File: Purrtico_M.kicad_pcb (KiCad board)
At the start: 2 copper layers, 100 x 60 mm, 120 parts, among them J1 Conn_02x05_Odd_Even, J2 Conn_01x02, J4 Conn_01x02, U1 OPA1679, U2 OPA1679, U3 OPA1679

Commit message: update high shelf
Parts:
- C20: value 470p -> 220p
- C31: value 4n7 -> 2n2
- C34: value 68n -> 22n

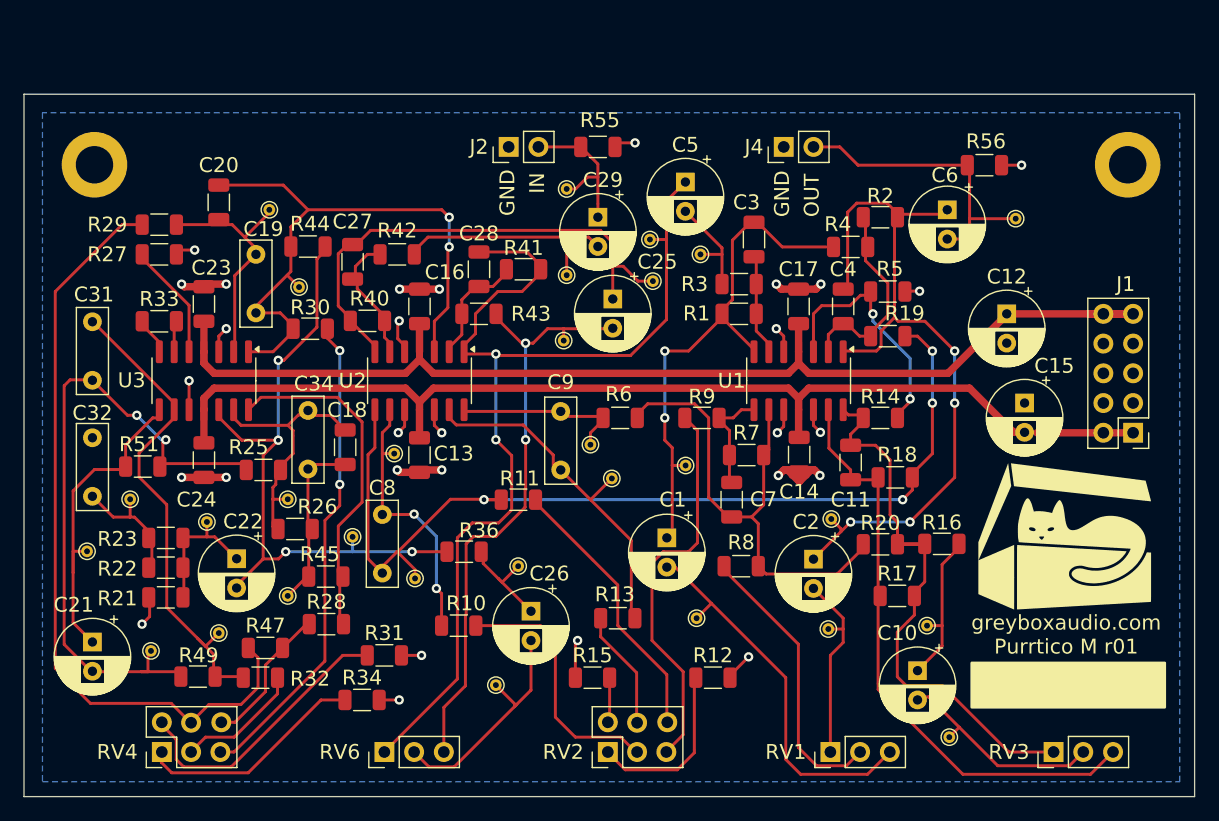
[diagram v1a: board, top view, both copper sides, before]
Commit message: added input gain control
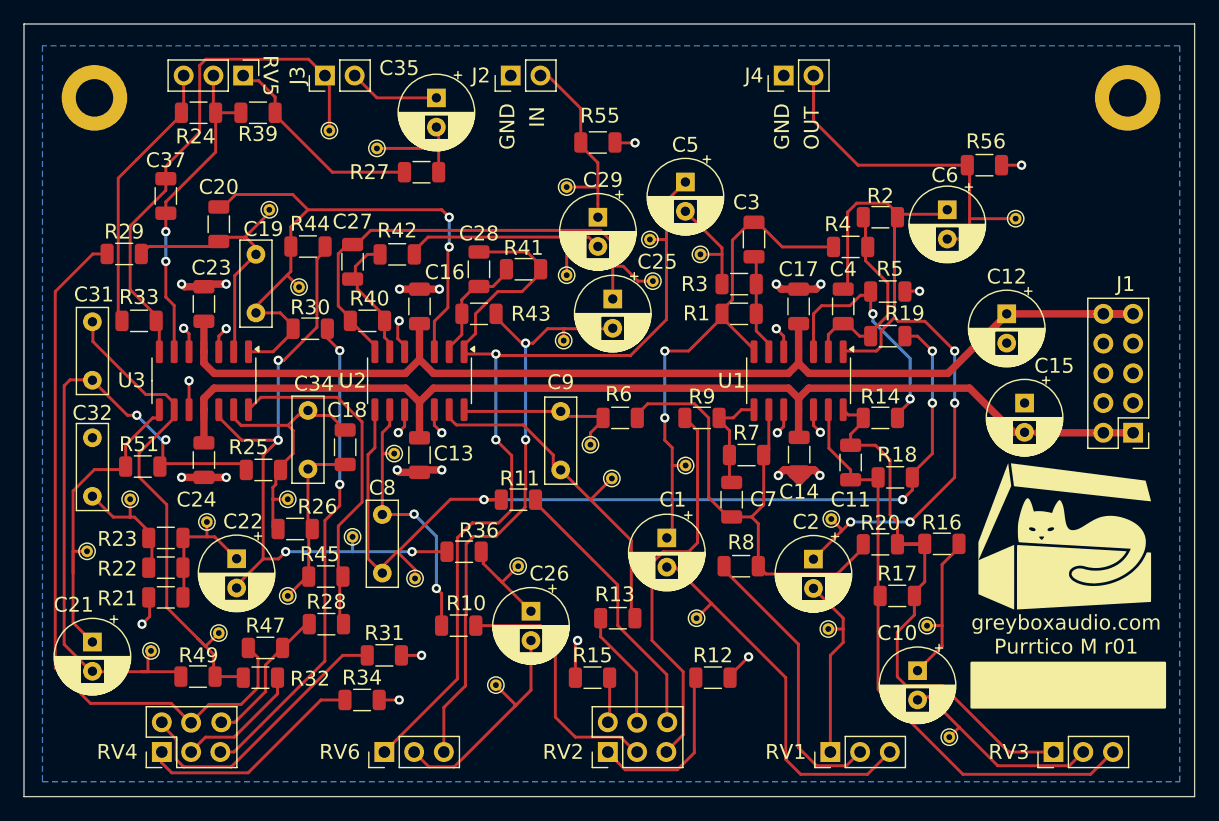
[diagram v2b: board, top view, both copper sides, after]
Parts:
- added C35: 100u, Capacitor_THT:CP_Radial_D6.3mm_P2.50mm, F.Cu at (113.0, 29.2)
- added C37: 22p, Capacitor_SMD:C_1206_3216Metric, F.Cu at (89.9, 37.6)
- added J3: Conn_01x02, Connector_PinHeader_2.54mm:PinHeader_1x02_P2.54mm_Vertical, F.Cu at (103.5, 27.3)
- added R24: 0R, Resistor_SMD:R_1206_3216Metric, F.Cu at (92.7, 30.5)
- added R39: 0R, Resistor_SMD:R_1206_3216Metric, F.Cu at (97.8, 30.5)
- added RV5: 5k log, Connector_PinHeader_2.54mm:PinHeader_1x03_P2.54mm_Vertical, F.Cu at (96.5, 27.3)
- added TP30: TestPoint, TestPoint:TestPoint_THTPad_D1.0mm_Drill0.5mm, F.Cu at (108.0, 33.5)
- added TP31: TestPoint, TestPoint:TestPoint_THTPad_D1.0mm_Drill0.5mm, F.Cu at (103.9, 32.0)
- R27, R33: value 0R -> 2k
- moved R27 23.5 mm to (111.8, 35.6)
- moved J2 6.10 mm to (119.4, 27.3)
- moved J4 6.09 mm to (142.7, 27.3)
- moved H1 5.71 mm to (83.8, 29.2)
- moved H2 5.71 mm to (172.1, 29.2)
- moved R29 3.91 mm to (86.4, 42.5)
- moved C20 1.87 mm to (94.4, 40.0)
- moved R33 1.73 mm to (87.6, 48.3), turned to 0 degrees
- moved R55 0.38 mm to (126.8, 33.0)
- moved TP1 0.16 mm to (124.2, 36.8)
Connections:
- R27 pad 1: GND -> Net-(C35-Pad2)
- R27 pad 2: Net-(U3B-+) -> Net-(R27-Pad2)
- R33 pad 1: Net-(U3B--) -> Net-(R24-Pad2)
- U3 pad 5: Net-(U3B-+) -> GND
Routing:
- net Net-(J3-Pin_1): track 2.07 -> 42.9 mm
- net Net-(U3B--): track 2.41 -> 27.6 mm, vias 0 -> 2
- net Net-(R24-Pad2): track 0.00 -> 22.5 mm
- net Net-(R27-Pad2): track 0.00 -> 17.7 mm
- net Net-(U3B-+): track 9.63 -> 0.00 mm
- net Net-(C35-Pad2): track 0.00 -> 8.93 mm
- net Net-(J3-Pin_2): track 0.00 -> 7.77 mm
- net Net-(J4-Pin_2): track 25.8 -> 30.6 mm
- net Net-(R29-Pad1): track 66.2 -> 62.2 mm
- net Net-(J2-Pin_2): track 13.3 -> 16.3 mm
- net Net-(U3A--): track 19.6 -> 21.6 mm
- net Net-(U3C--): track 40.4 -> 41.4 mm
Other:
- board size 100 x 60 mm -> 100 x 66 mm

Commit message: added 0R for mounting holes
as well as some small layout refinements
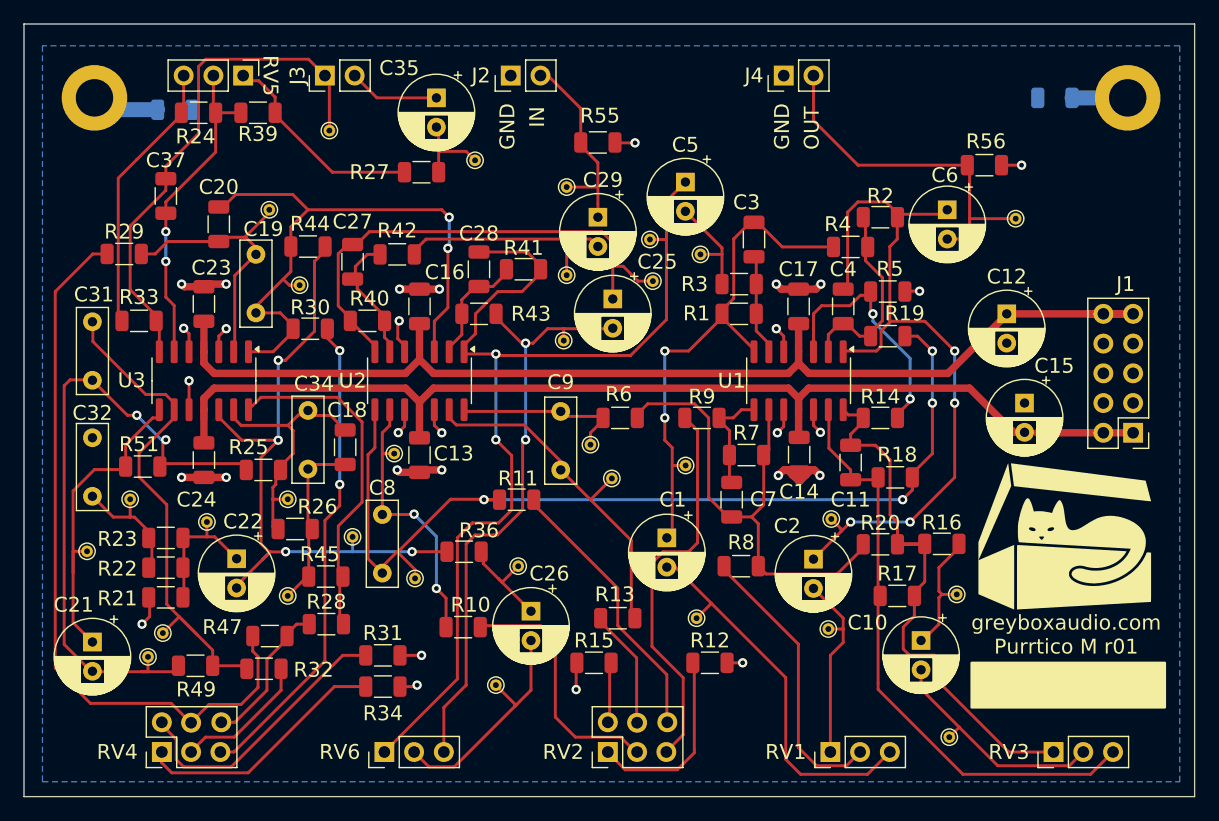
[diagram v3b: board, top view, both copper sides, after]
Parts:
- added R35: 0R, Resistor_SMD:R_1206_3216Metric, B.Cu at (90.7, 30.2)
- added R37: 0R, Resistor_SMD:R_1206_3216Metric, B.Cu at (165.9, 29.2)
- moved TP30 8.44 mm to (116.3, 34.5)
- moved TP20 4.78 mm to (89.7, 74.9)
- moved TP19 3.68 mm to (157.5, 71.6)
- moved C10 2.59 mm to (154.4, 75.6)
- moved R34 2.11 mm to (108.5, 79.5)
- moved R12 1.30 mm to (136.4, 77.5)
- moved R15 1.28 mm to (126.5, 77.5)
- moved R47 1.09 mm to (98.8, 75.2)
- moved R49 0.95 mm to (92.5, 77.7)
- moved R32 0.82 mm to (98.3, 78.0)
- moved TP17 0.57 mm to (88.4, 77.0)
- moved R10 0.40 mm to (115.3, 74.4)
- moved TP22 0.17 mm to (101.3, 45.2)
- moved R11 0.14 mm to (119.9, 63.5)
- moved R31 0.13 mm to (108.5, 76.8)
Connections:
- H1 pad 1: GND -> Net-(H1-Pad1)
- H2 pad 1: GND -> Net-(H2-Pad1)
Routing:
- net Net-(H2-Pad1): track 0.00 -> 4.76 mm
- net Net-(H1-Pad1): track 0.00 -> 4.38 mm
- net Net-(C10-Pad1): track 13.3 -> 10.9 mm
- net Net-(R34-Pad2): track 19.5 -> 21.8 mm
- net GND: track 61.3 -> 59.3 mm
- net Net-(C35-Pad2): track 8.93 -> 7.34 mm
- net Net-(C10-Pad2): track 18.3 -> 19.8 mm
- net Net-(R12-Pad2): track 15.0 -> 16.2 mm
- net Net-(U3C--): track 41.4 -> 42.6 mm
- net Net-(R15-Pad2): track 3.62 -> 4.76 mm
- net Net-(C11-Pad1): track 48.1 -> 47.1 mm
- net Net-(R32-Pad2): track 10.9 -> 11.7 mm
- net Net-(R29-Pad1): track 62.2 -> 63.0 mm
- net Net-(U3D-+): track 54.6 -> 55.4 mm
- net Net-(R10-Pad1): track 22.0 -> 21.4 mm

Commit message: update pcb
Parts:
- moved C15 1.35 mm to (161.9, 55.3)
- moved C12 0.46 mm to (161.3, 47.7)
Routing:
- net -15V: track 92.2 -> 93.2 mm
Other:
- board text added: "V+"
- board text added: "V-"

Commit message: update potentiometer values
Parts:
- RV1, RV6: value 5k -> 5k log
- RV2, RV4: value 10k -> 10k log
- RV3: value 10k -> 10k lin

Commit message: added gerber files
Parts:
- moved RV5 5.08 mm to (91.4, 27.3), turned to 90 degrees
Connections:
- RV5 pad 1: Net-(R27-Pad2) -> Net-(R24-Pad2)
- RV5 pad 3: Net-(R24-Pad2) -> Net-(R27-Pad2)
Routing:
- net Net-(R27-Pad2): track 17.7 -> 16.9 mm
